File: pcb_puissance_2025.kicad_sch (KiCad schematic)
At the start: 36 parts, among them J1 1755736, J2 1755736, J3 1755736, J4 1755736, J5 1755736, J6 1755736

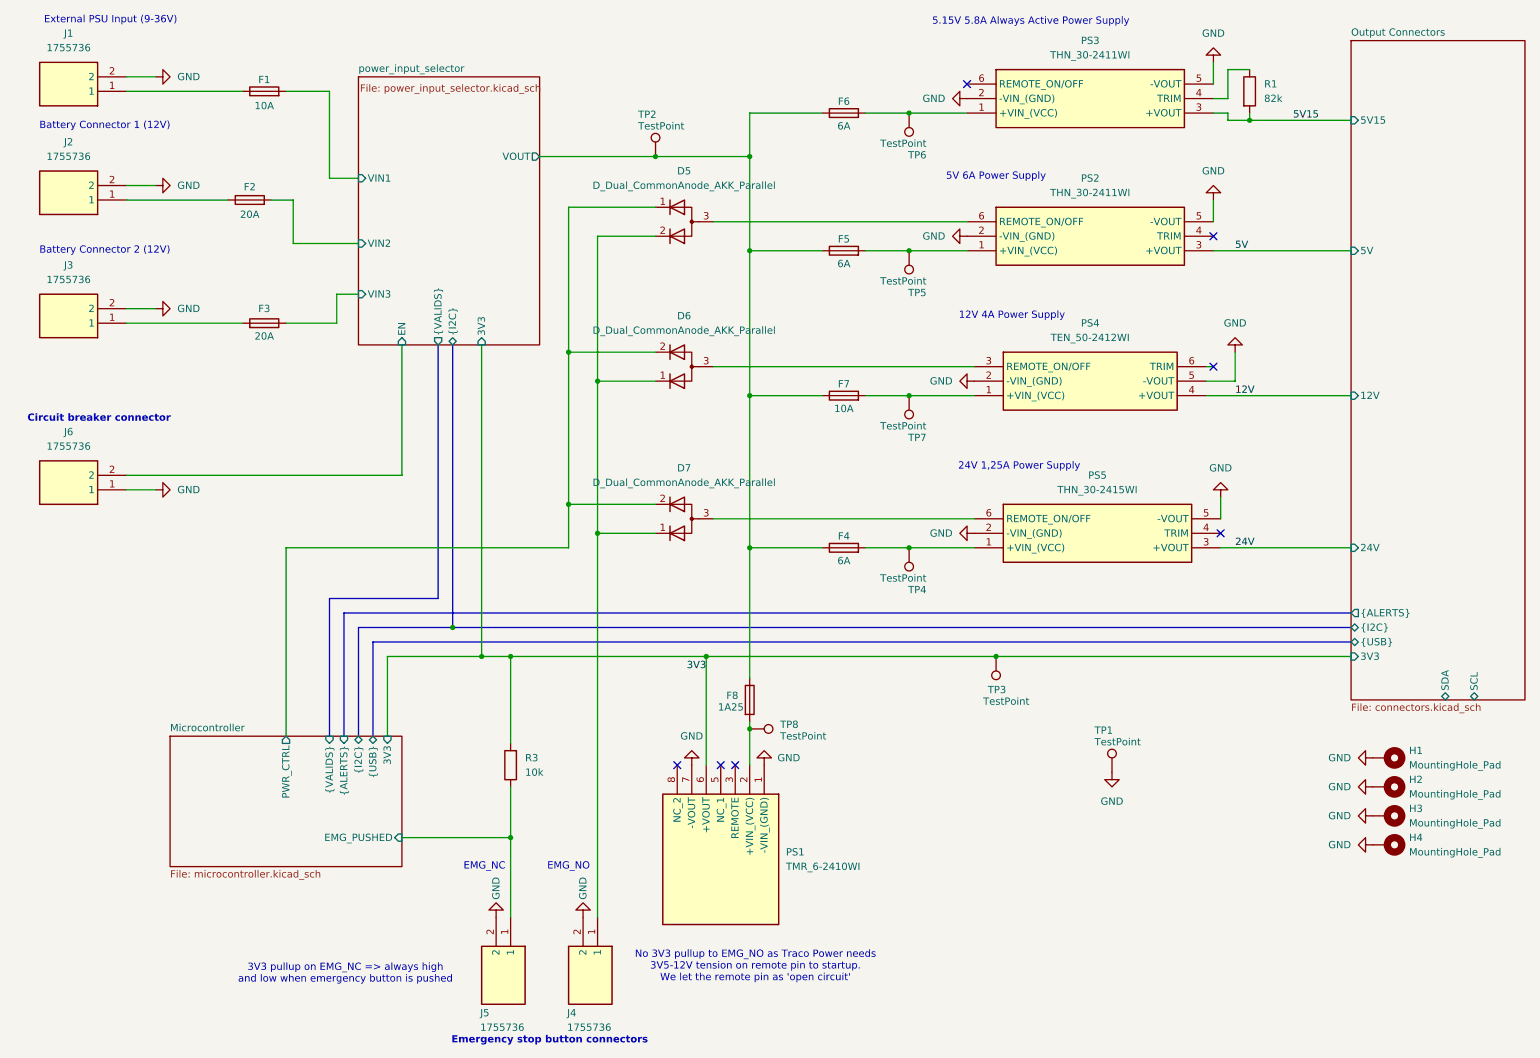
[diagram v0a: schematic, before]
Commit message: Correctifs et améliorations + passage à KiCad V9
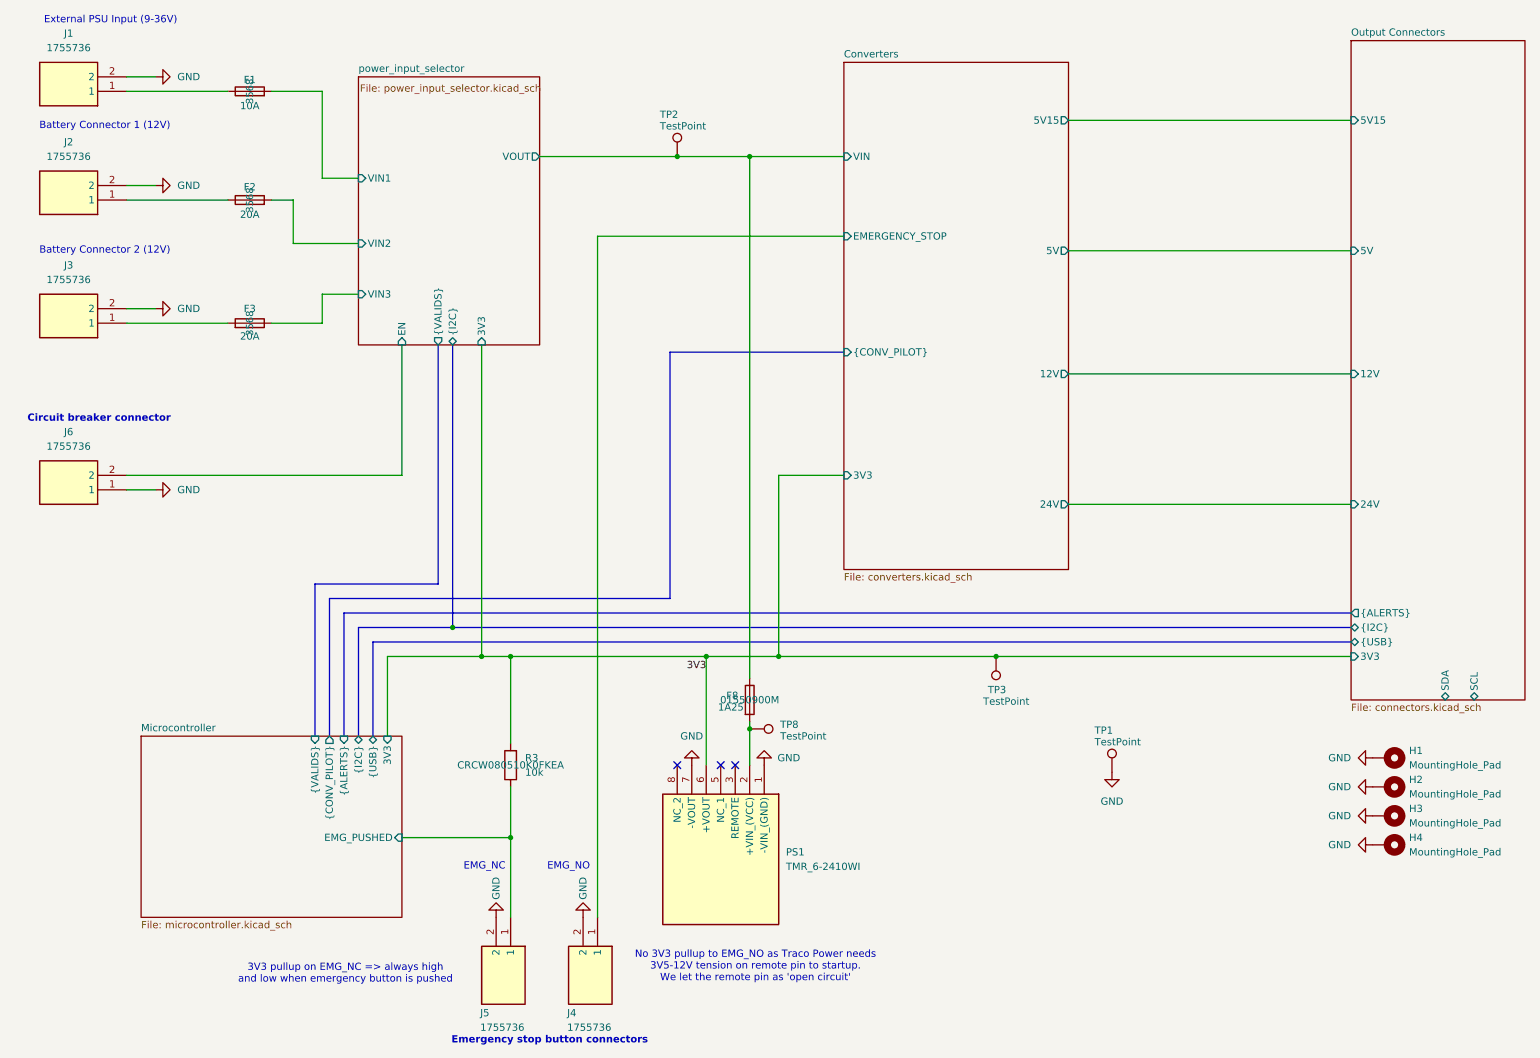
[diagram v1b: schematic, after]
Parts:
- removed D5, D6, D7: D_Dual_CommonAnode_AKK_Parallel, Package_TO_SOT_SMD:TSOT-23_HandSoldering, symbol Device:D_Dual_CommonAnode_AKK_Parallel
- removed F4, F5, F6: 6A, Modelec:01550900M, symbol Device:Fuse
- removed F7: 10A, Modelec:01550900M, symbol Device:Fuse
- removed PS2, PS3: THN_30-2411WI, THN301211, symbol Modelec:THN_30-1211
- removed PS4: TEN_50-2412WI, TEN_50-2411, symbol Modelec:TEN_50-2412WI
- removed PS5: THN_30-2415WI, THN301211, symbol Modelec:THN_30-1211
- removed R1: 82k, Resistor_SMD:R_0805_2012Metric_Pad1.20x1.40mm_HandSolder, symbol Device:R
- removed TP4, TP5, TP6, TP7: TestPoint, TestPoint:TestPoint_Pad_D1.5mm, symbol Connector:TestPoint
- F1, F2, F3: Manufacturer_Part_Number (none) -> 3568
- F8: Manufacturer_Part_Number (none) -> 01550900M
- PS1: Manufacturer_Part_Number TMR 6-0510 -> TMR_6-2410WI
- R3: Manufacturer_Part_Number (none) -> CRCW080510K0FKEA
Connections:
- net Converters/EMERGENCY_STOP: now reaches J4.1
- net power_input_selector/VOUT renamed Converters/VIN
- no-connect marks 7 -> 3
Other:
- added sheet Converters (converters.kicad_sch)
- sheet Microcontroller ports: added {CONV_PILOT}; removed PWR_CTRL
- note removed: "12V 4A Power Supply"
- note removed: "24V 1,25A Power Supply"
- note removed: "5.15V 5.8A Always Active Power Supply"
- note removed: "5V 6A Power Supply"
- moved on the sheet: F1, F3
